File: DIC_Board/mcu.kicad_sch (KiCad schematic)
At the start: 61 parts, among them J1 DM3AT-SF-PEJM5, J2 Conn_ARM_JTAG_SWD_10, SW1 SW_Push, U1 STM32L476ZGTx, U2 AB-RTCMC-32.768kHz-EOA9-S3, U3 APS6404L-3SQRX-SN, Y1 ABM8AAIG-8.000MHz-V2R-T3, Y2 ABS06-107-32.768KHZ-T

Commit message: Checkpoint current schematic state
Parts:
- added P1: USB_C_Plug_USB2.0, symbol Connector:USB_C_Plug_USB2.0
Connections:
- net GND: now also P1.A1 (GND), P1.A12 (GND), P1.B1 (GND), P1.B12 (GND), P1.SH (SHIELD)
- net USB_OTG_FS_DM: now also P1.A7 (D-)
- net USB_OTG_FS_DP: now also P1.A6 (D+)
- new net: P1.A4 (VBUS), P1.A9 (VBUS), P1.B4 (VBUS), P1.B9 (VBUS)
- no-connect marks 0 -> 3
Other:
- note added: "USB"
- moved on the sheet: C21, C30, C31, J1, J2, JP1, R1, R10, R11, R12, R13, R14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

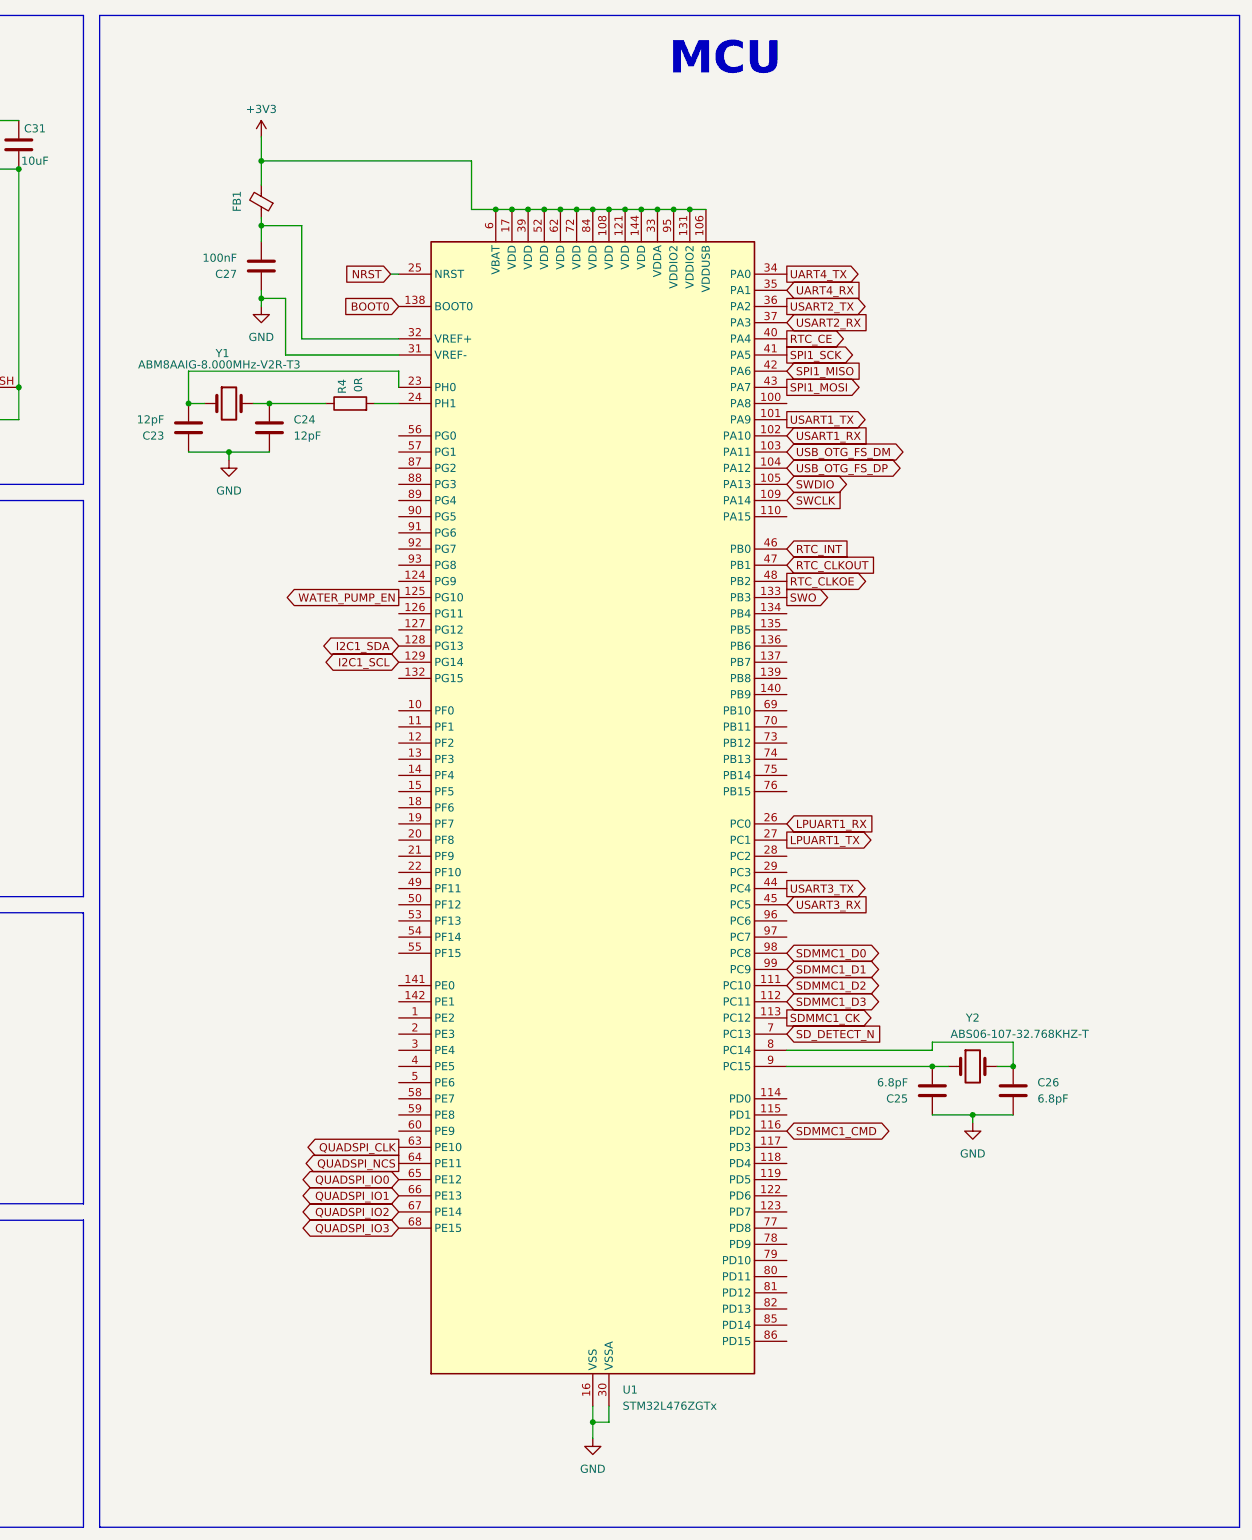
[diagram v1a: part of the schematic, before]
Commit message: Synchronize schematic hierarchy and MCU pin map
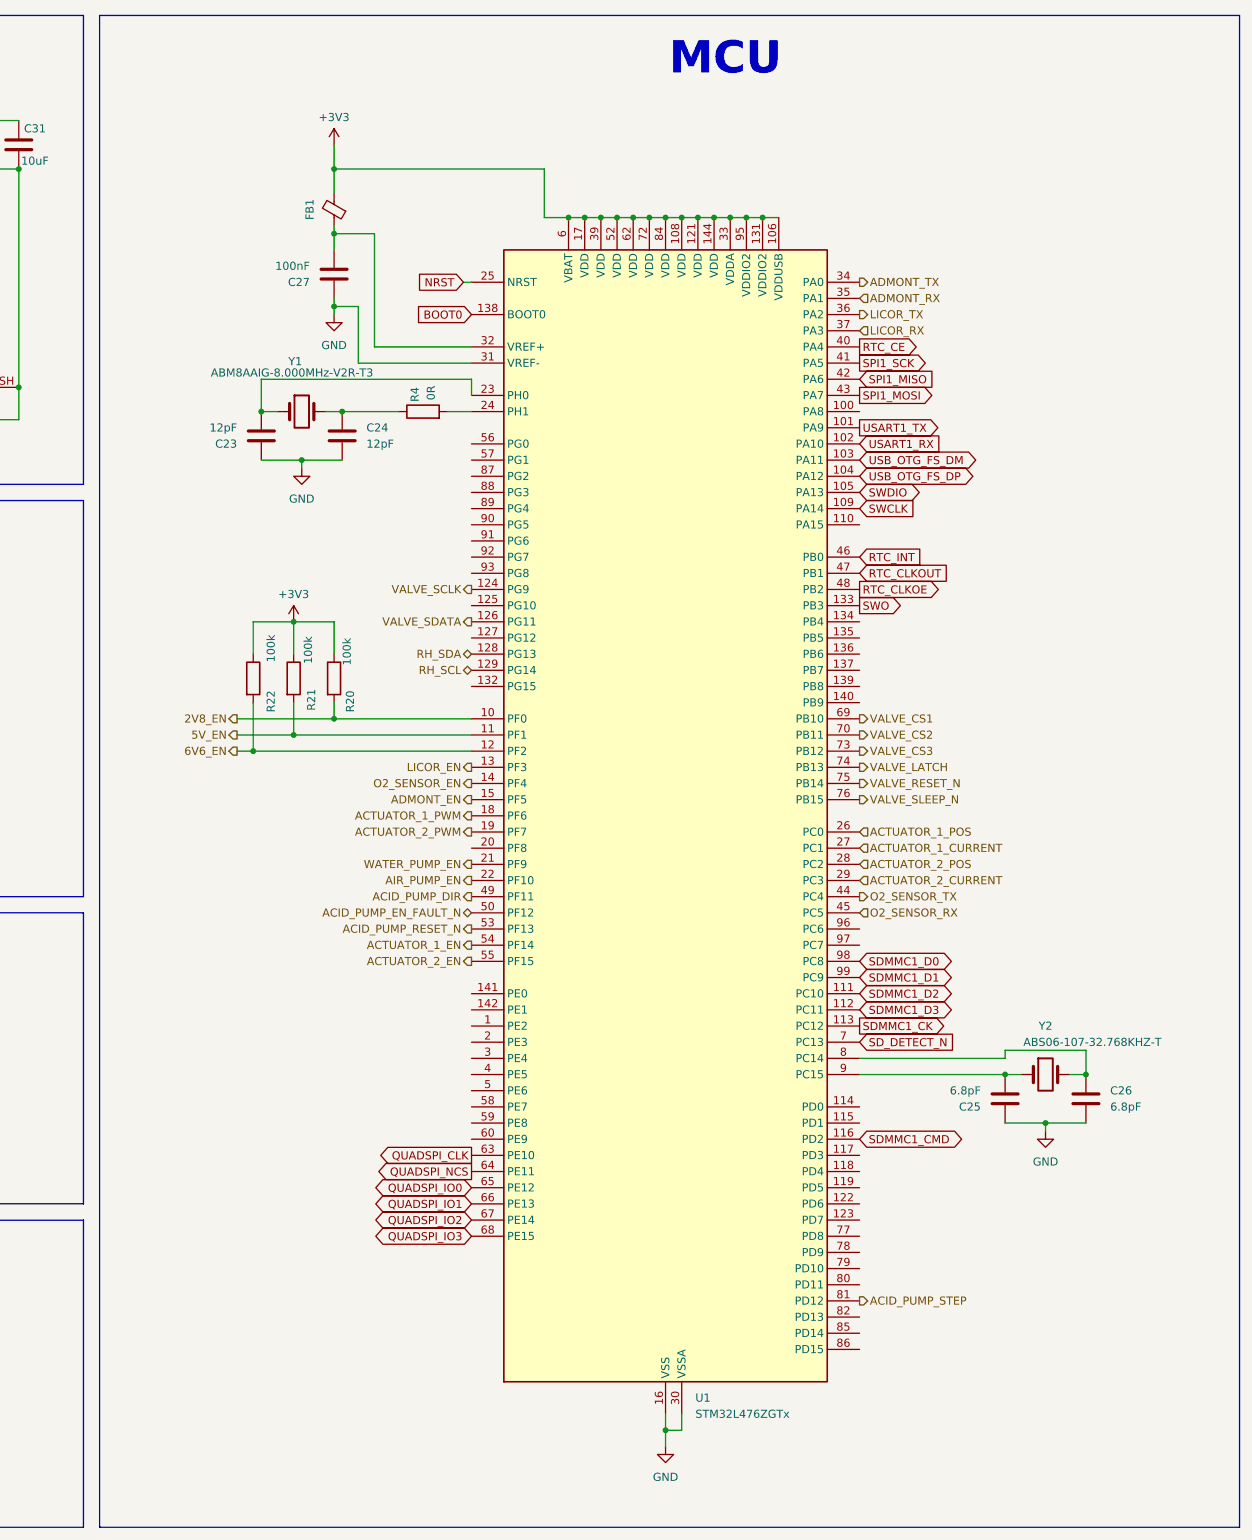
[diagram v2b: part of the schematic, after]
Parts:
- added R20, R21, R22: 100k, Resistor_SMD:R_0402_1005Metric, symbol Device:R
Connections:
- net +3V3: now also R20.1, R21.1, R22.1
- net WATER_PUMP_EN: now also U1.21 (PF9); no longer U1.125 (PG10)
- net 2V8_EN: now reaches U1.10 (PF0)
- net 2V8_EN: now also R20.2
- net 5V_EN: now reaches U1.11 (PF1)
- net 5V_EN: now also R21.2
- net 6V6_EN: now reaches U1.12 (PF2)
- net 6V6_EN: now also R22.2
- net VALVE_SCLK: now reaches U1.124 (PG9)
- net VALVE_SDATA: now reaches U1.126 (PG11)
- net LICOR_EN: now reaches U1.13 (PF3)
- net O2_SENSOR_EN: now reaches U1.14 (PF4)
- net ADMONT_EN: now reaches U1.15 (PF5)
- net ACTUATOR_1_PWM: now reaches U1.18 (PF6)
- net ACTUATOR_2_PWM: now reaches U1.19 (PF7)
- net AIR_PUMP_EN: now reaches U1.22 (PF10)
- net ACTUATOR_2_POS: now reaches U1.28 (PC2)
- net ACTUATOR_2_CURRENT: now reaches U1.29 (PC3)
- net ACID_PUMP_DIR: now reaches U1.49 (PF11)
- net ACID_PUMP_EN_FAULT_N: now reaches U1.50 (PF12)
- net ACID_PUMP_RESET_N: now reaches U1.53 (PF13)
- net ACTUATOR_1_EN: now reaches U1.54 (PF14)
- net ACTUATOR_2_EN: now reaches U1.55 (PF15)
- net VALVE_CS1: now reaches U1.69 (PB10)
- net VALVE_CS2: now reaches U1.70 (PB11)
- net VALVE_CS3: now reaches U1.73 (PB12)
- net VALVE_LATCH: now reaches U1.74 (PB13)
- net VALVE_RESET_N: now reaches U1.75 (PB14)
- net VALVE_SLEEP_N: now reaches U1.76 (PB15)
- net ACID_PUMP_STEP: now reaches U1.81 (PD12)
- net I2C1_SCL renamed RH_SCL
- net I2C1_SDA renamed RH_SDA
- net LPUART1_RX renamed ACTUATOR_1_POS
- net LPUART1_TX renamed ACTUATOR_1_CURRENT
- net UART4_RX renamed ADMONT_RX
- net UART4_TX renamed ADMONT_TX
- net USART2_RX renamed LICOR_RX
- net USART2_TX renamed LICOR_TX
- net USART3_RX renamed O2_SENSOR_RX
- net USART3_TX renamed O2_SENSOR_TX
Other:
- moved on the sheet: C23, C24, C25, C26, C27, FB1, R4, U1, Y1, Y2

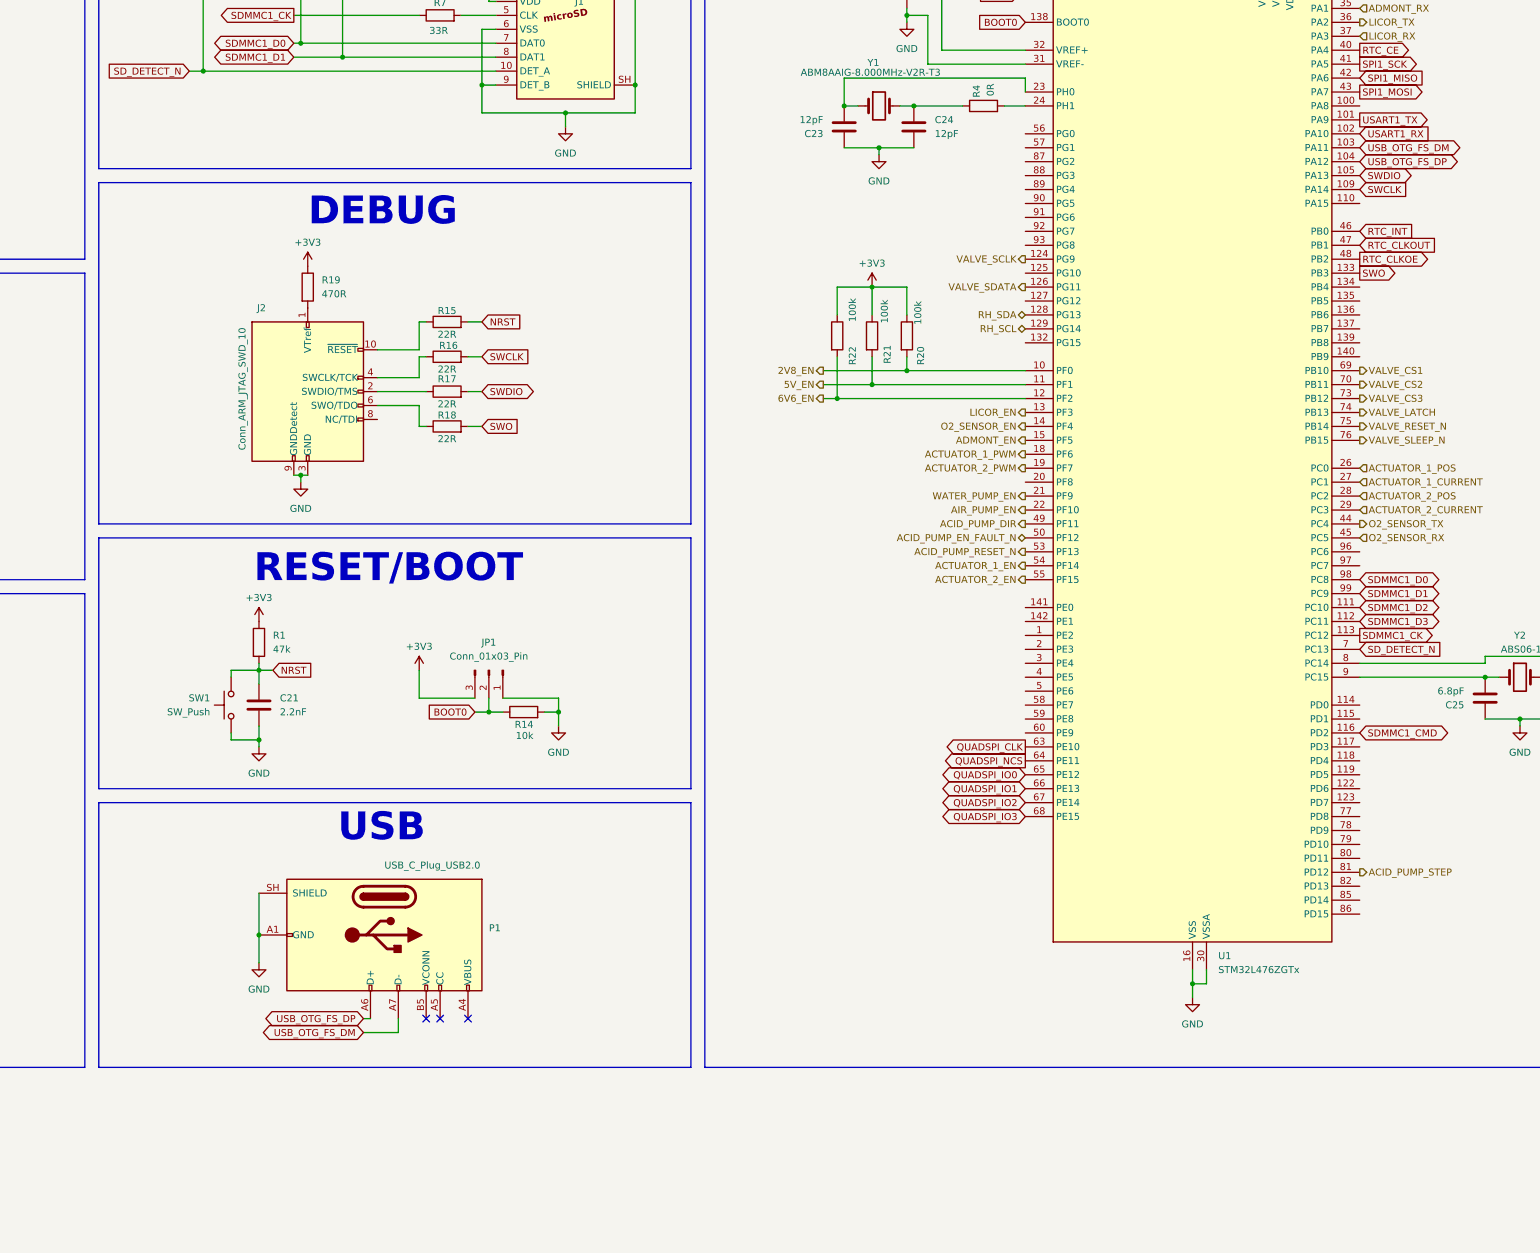
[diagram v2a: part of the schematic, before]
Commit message: Synchronize power, communications, and MCU configuration
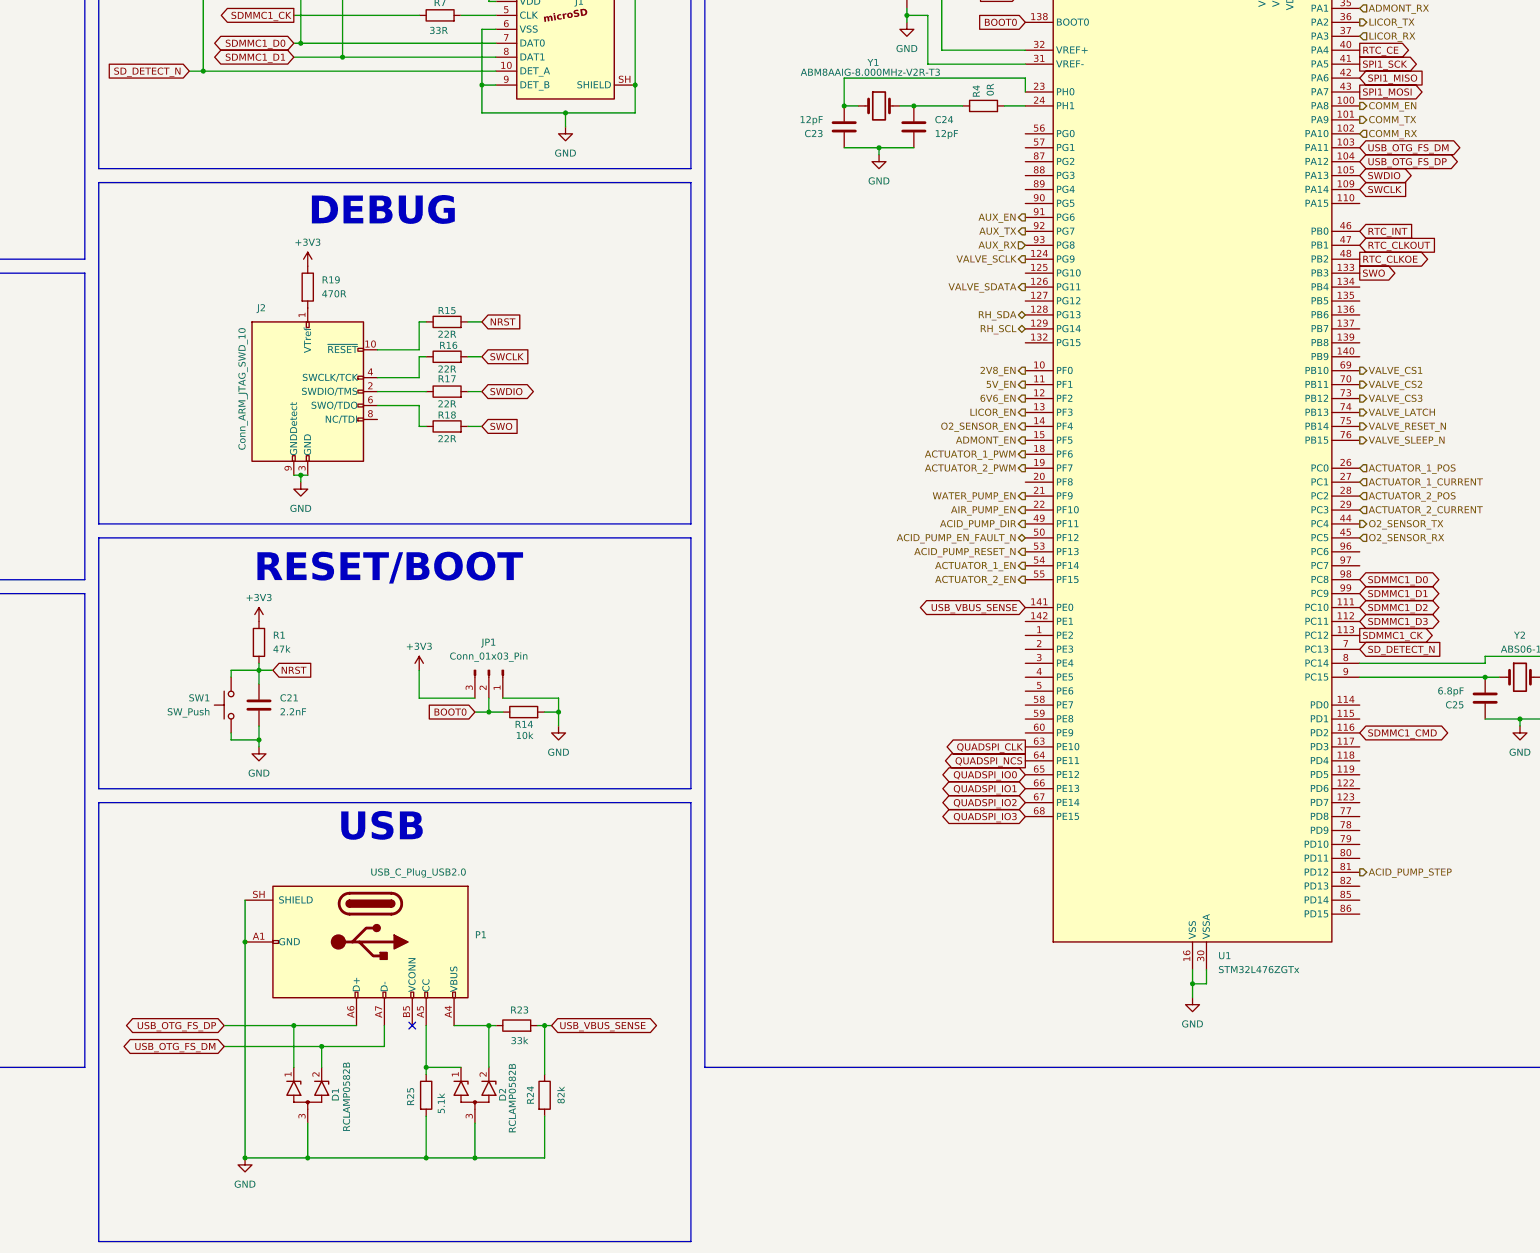
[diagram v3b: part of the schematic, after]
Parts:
- removed R20, R21, R22: 100k, Resistor_SMD:R_0402_1005Metric, symbol Device:R
- added D1, D2: RCLAMP0582B, Package_TO_SOT_SMD:SOT-523, symbol Power_Protection:RCLAMP0582B
- added R23: 33k, Resistor_SMD:R_0402_1005Metric, symbol Device:R
- added R24: 82k, Resistor_SMD:R_0402_1005Metric, symbol Device:R
- added R25: 5.1k, Resistor_SMD:R_0402_1005Metric, symbol Device:R
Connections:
- net GND: now also D1.3 (A), D2.3 (A), R24.2, R25.2
- net USB_OTG_FS_DM: now also D1.2 (K2)
- net USB_OTG_FS_DP: now also D1.1 (K1)
- net at P1.A4 (VBUS), P1.A9 (VBUS), P1.B4 (VBUS)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: now also D2.2 (K2), R23.1
- net at P1.A5 (CC): now also D2.1 (K1), R25.1
- net COMM_EN: now reaches U1.100 (PA8)
- net USB_VBUS_SENSE: now reaches U1.141 (PE0)
- net USB_VBUS_SENSE: now also R23.2, R24.1
- net AUX_EN: now reaches U1.91 (PG6)
- net AUX_TX: now reaches U1.92 (PG7)
- net AUX_RX: now reaches U1.93 (PG8)
- net USART1_RX renamed COMM_RX
- net USART1_TX renamed COMM_TX
- no-connect marks 3 -> 1
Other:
- moved on the sheet: P1
